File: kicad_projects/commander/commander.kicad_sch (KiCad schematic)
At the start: 27 parts, among them J1 right input IDC14, J10 Conn_02x01, J11 Conn_02x01, J12 Conn_02x01, J13 Conn_02x01, J2 left input IDC14, J3 VIK FCC 12, J4 TPS pinout, J5 DS1020-12-6VBT1A-R, J6 PSP 3000 connector SFV4R-4STB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, J7 PSP 2000 raw pins out, J8 debug out, J9 HC-FPC-05-09-4RLTAG, Q1 AO3401A, Q2 NPN - MMBT2222A, SW1 RESET_SWITCH, SW2 SW_Push, SW3 SW_Push, SW4 SW_Push, U1 Pico

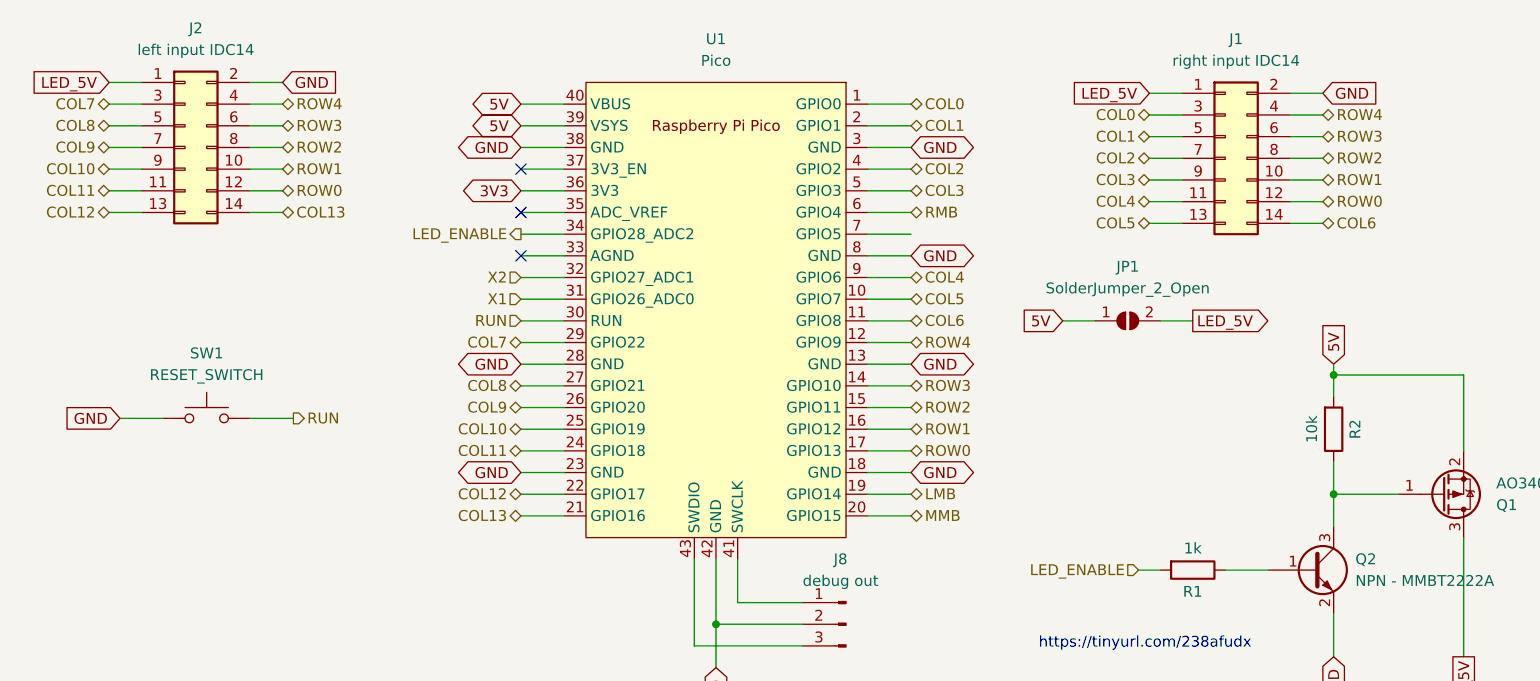
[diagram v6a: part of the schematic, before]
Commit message: Correct Column net names
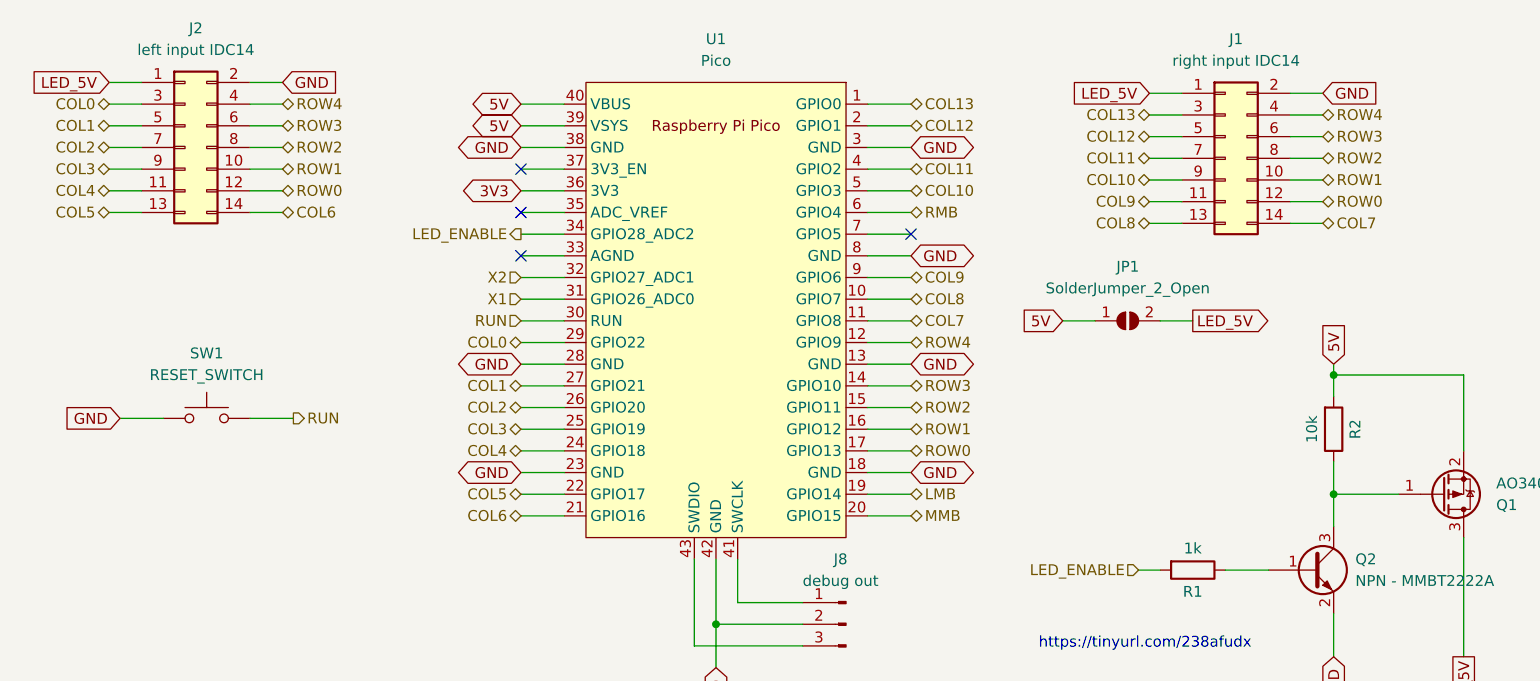
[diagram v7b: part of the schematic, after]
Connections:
- net COL0: now also J2.3 (Pin_3), U1.29 (GPIO22); no longer J1.3 (Pin_3), U1.1 (GPIO0)
- net COL1: now also J2.5 (Pin_5), U1.27 (GPIO21); no longer J1.5 (Pin_5), U1.2 (GPIO1)
- net COL10: now also J1.9 (Pin_9), U1.5 (GPIO3); no longer J2.9 (Pin_9), U1.25 (GPIO19)
- net COL11: now also J1.7 (Pin_7), U1.4 (GPIO2); no longer J2.11 (Pin_11), U1.24 (GPIO18)
- net COL12: now also J1.5 (Pin_5), U1.2 (GPIO1); no longer J2.13 (Pin_13), U1.22 (GPIO17)
- net COL13: now also J1.3 (Pin_3), U1.1 (GPIO0); no longer J2.14 (Pin_14), U1.21 (GPIO16)
- net COL2: now also J2.7 (Pin_7), U1.26 (GPIO20); no longer J1.7 (Pin_7), U1.4 (GPIO2)
- net COL3: now also J2.9 (Pin_9), U1.25 (GPIO19); no longer J1.9 (Pin_9), U1.5 (GPIO3)
- net COL4: now also J2.11 (Pin_11), U1.24 (GPIO18); no longer J1.11 (Pin_11), U1.9 (GPIO6)
- net COL5: now also J2.13 (Pin_13), U1.22 (GPIO17); no longer J1.13 (Pin_13), U1.10 (GPIO7)
- net COL6: now also J2.14 (Pin_14), U1.21 (GPIO16); no longer J1.14 (Pin_14), U1.11 (GPIO8)
- net COL7: now also J1.14 (Pin_14), U1.11 (GPIO8); no longer J2.3 (Pin_3), U1.29 (GPIO22)
- net COL8: now also J1.13 (Pin_13), U1.10 (GPIO7); no longer J2.5 (Pin_5), U1.27 (GPIO21)
- net COL9: now also J1.11 (Pin_11), U1.9 (GPIO6); no longer J2.7 (Pin_7), U1.26 (GPIO20)
- no-connect marks 15 -> 16
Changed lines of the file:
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@@
+	)
+	(no_connect
+		(at 118.11 43.18)
 	)
 	(no_connect
@@
 		)
 	)
-	(hierarchical_label "COL11"
+	(hierarchical_label "COL4"
 		(shape bidirectional)
 		(at 72.39 68.58 180)
@@
 		)
 	)
-	(hierarchical_label "COL11"
+	(hierarchical_label "COL4"
 		(shape bidirectional)
 		(at 24.13 38.1 180)
@@
 		)
 	)
-	(hierarchical_label "COL8"
+	(hierarchical_label "COL1"
 		(shape bidirectional)
 		(at 24.13 30.48 180)
@@
 		)
 	)
-	(hierarchical_label "COL1"
+	(hierarchical_label "COL12"
 		(shape bidirectional)
 		(at 146.05 31.75 180)
@@
 		)
 	)
-	(hierarchical_label "COL9"
+	(hierarchical_label "COL2"
 		(shape bidirectional)
 		(at 24.13 33.02 180)
@@
 		)
 	)
-	(hierarchical_label "COL0"
+	(hierarchical_label "COL13"
 		(shape bidirectional)
 		(at 146.05 29.21 180)
@@
 		)
 	)
-	(hierarchical_label "COL13"
+	(hierarchical_label "COL6"
 		(shape bidirectional)
 		(at 44.45 40.64 0)
@@
 		)
 	)
-	(hierarchical_label "COL10"
+	(hierarchical_label "COL3"
 		(shape bidirectional)
 		(at 72.39 66.04 180)
@@
 		)
 	)
-	(hierarchical_label "COL7"
+	(hierarchical_label "COL0"
 		(shape bidirectional)
 		(at 24.13 27.94 180)
@@
 		)
 	)
-	(hierarchical_label "COL8"
+	(hierarchical_label "COL1"
 		(shape bidirectional)
 		(at 72.39 60.96 180)
@@
 		)
 	)
-	(hierarchical_label "COL12"
+	(hierarchical_label "COL5"
 		(shape bidirectional)
 		(at 24.13 40.64 180)
@@
 		)
 	)
-	(hierarchical_label "COL4"
+	(hierarchical_label "COL9"
 		(shape bidirectional)
 		(at 118.11 48.26 0)
@@
 		)
 	)
-	(hierarchical_label "COL12"
+	(hierarchical_label "COL5"
 		(shape bidirectional)
 		(at 72.39 73.66 180)
@@
 		)
 	)
-	(hierarchical_label "COL0"
+	(hierarchical_label "COL13"
 		(shape bidirectional)
 		(at 118.11 27.94 0)
@@
 		)
 	)
-	(hierarchical_label "COL10"
+	(hierarchical_label "COL3"
 		(shape bidirectional)
 		(at 24.13 35.56 180)
@@
 		)
 	)
-	(hierarchical_label "COL1"
+	(hierarchical_label "COL12"
 		(shape bidirectional)
 		(at 118.11 30.48 0)
@@
 		)
 	)
-	(hierarchical_label "COL9"
+	(hierarchical_label "COL2"
 		(shape bidirectional)
 		(at 72.39 63.5 180)
@@
 		)
 	)
-	(hierarchical_label "COL13"
+	(hierarchical_label "COL6"
 		(shape bidirectional)
 		(at 72.39 76.2 180)
@@
 		)
 	)
-	(hierarchical_label "COL2"
+	(hierarchical_label "COL11"
 		(shape bidirectional)
 		(at 146.05 34.29 180)
@@
 		)
 	)
-	(hierarchical_label "COL6"
+	(hierarchical_label "COL7"
 		(shape bidirectional)
 		(at 118.11 53.34 0)
@@
 		)
 	)
-	(hierarchical_label "COL6"
+	(hierarchical_label "COL7"
 		(shape bidirectional)
 		(at 166.37 41.91 0)
@@
 		)
 	)
-	(hierarchical_label "COL5"
+	(hierarchical_label "COL8"
 		(shape bidirectional)
 		(at 118.11 50.8 0)
@@
 		)
 	)
-	(hierarchical_label "COL2"
+	(hierarchical_label "COL11"
 		(shape bidirectional)
 		(at 118.11 35.56 0)
@@
 		)
 	)
-	(hierarchical_label "COL7"
+	(hierarchical_label "COL0"
 		(shape bidirectional)
 		(at 72.39 55.88 180)
@@
 		)
 	)
-	(hierarchical_label "COL3"
+	(hierarchical_label "COL10"
 		(shape bidirectional)
 		(at 118.11 38.1 0)
@@
 		)
 	)
-	(hierarchical_label "COL4"
+	(hierarchical_label "COL9"
 		(shape bidirectional)
 		(at 146.05 39.37 180)
@@
 		)
 	)
-	(hierarchical_label "COL5"
+	(hierarchical_label "COL8"
 		(shape bidirectional)
 		(at 146.05 41.91 180)
@@
 		)
 	)
-	(hierarchical_label "COL3"
+	(hierarchical_label "COL10"
 		(shape bidirectional)
 		(at 146.05 36.83 180)
